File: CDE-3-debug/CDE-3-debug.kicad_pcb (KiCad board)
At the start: 2 copper layers, 101 x 86.4 mm, 79 parts

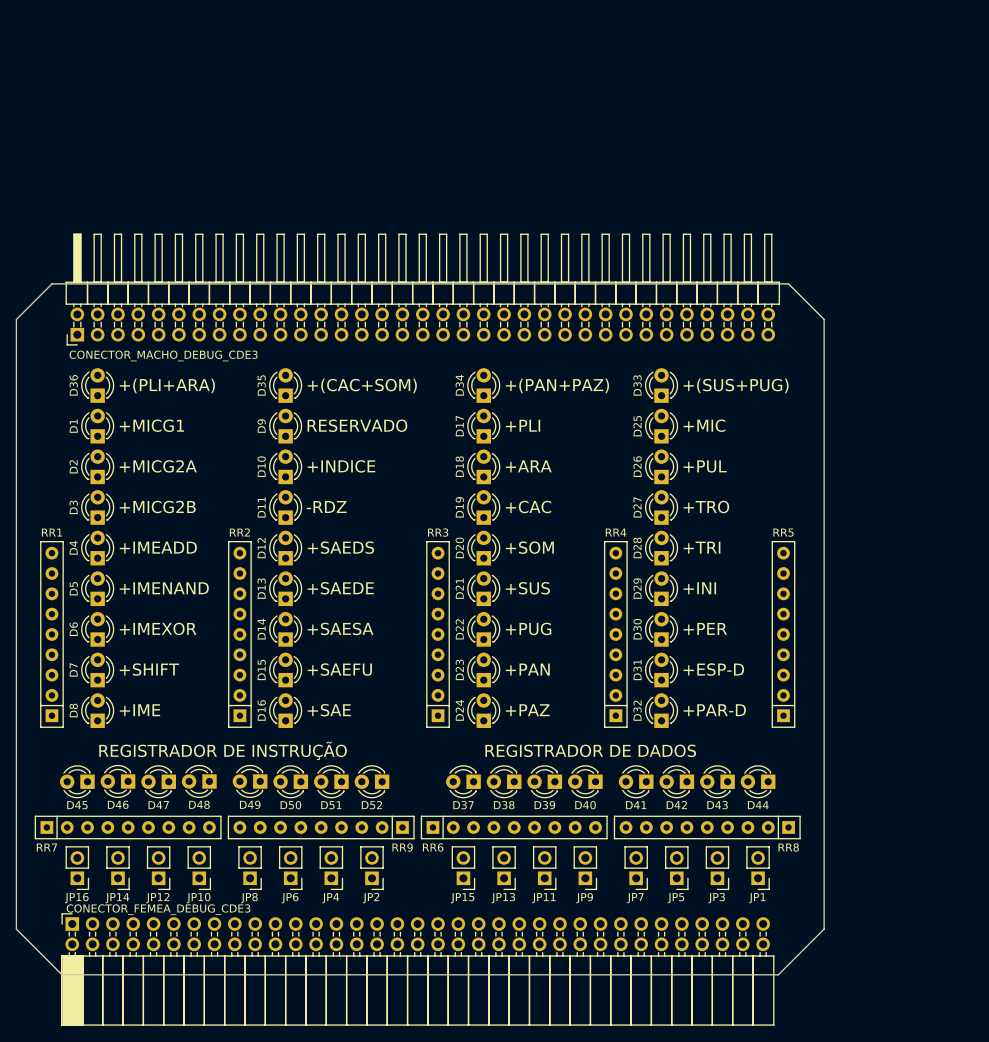
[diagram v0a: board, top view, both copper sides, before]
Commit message: trocando posição dos conectores macho/femea
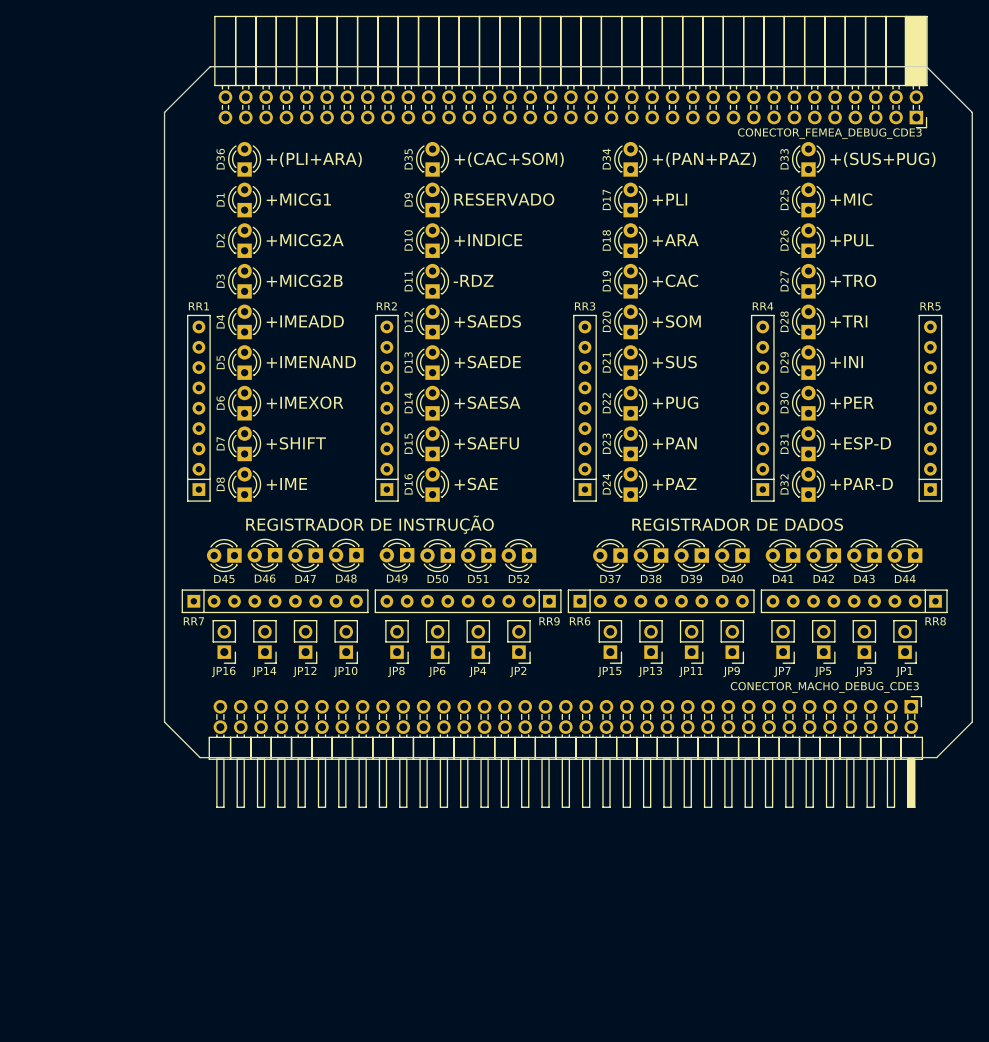
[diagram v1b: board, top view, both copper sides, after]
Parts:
- moved CONECTOR_FEMEA_DEBUG_CDE3 145.9 mm to (156.3, 80.8), turned to 270 degrees
- moved CONECTOR_MACHO_DEBUG_CDE3 114.1 mm to (155.7, 154.5), turned to 270 degrees
- moved JP5 33.7 mm to (144.7, 147.6)
- moved D25 33.7 mm to (142.8, 92.4)
- moved D26 33.7 mm to (142.8, 97.5)
- moved D27 33.7 mm to (142.8, 102.5)
- moved D30 33.7 mm to (142.8, 117.8)
- moved D32 33.7 mm to (142.8, 127.9)
- moved D37 33.7 mm to (119.3, 135.6)
- moved D38 33.7 mm to (124.4, 135.6)
- moved D39 33.7 mm to (129.5, 135.6)
- moved D41 33.7 mm to (140.9, 135.6)
- moved D43 33.7 mm to (151.1, 135.6)
- moved D44 33.7 mm to (156.2, 135.6)
- moved D45 33.7 mm to (71.1, 135.6)
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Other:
- outline, holes or cut-outs redrawn

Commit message: improvements to the CDE-3 and CDE-3-debug boards
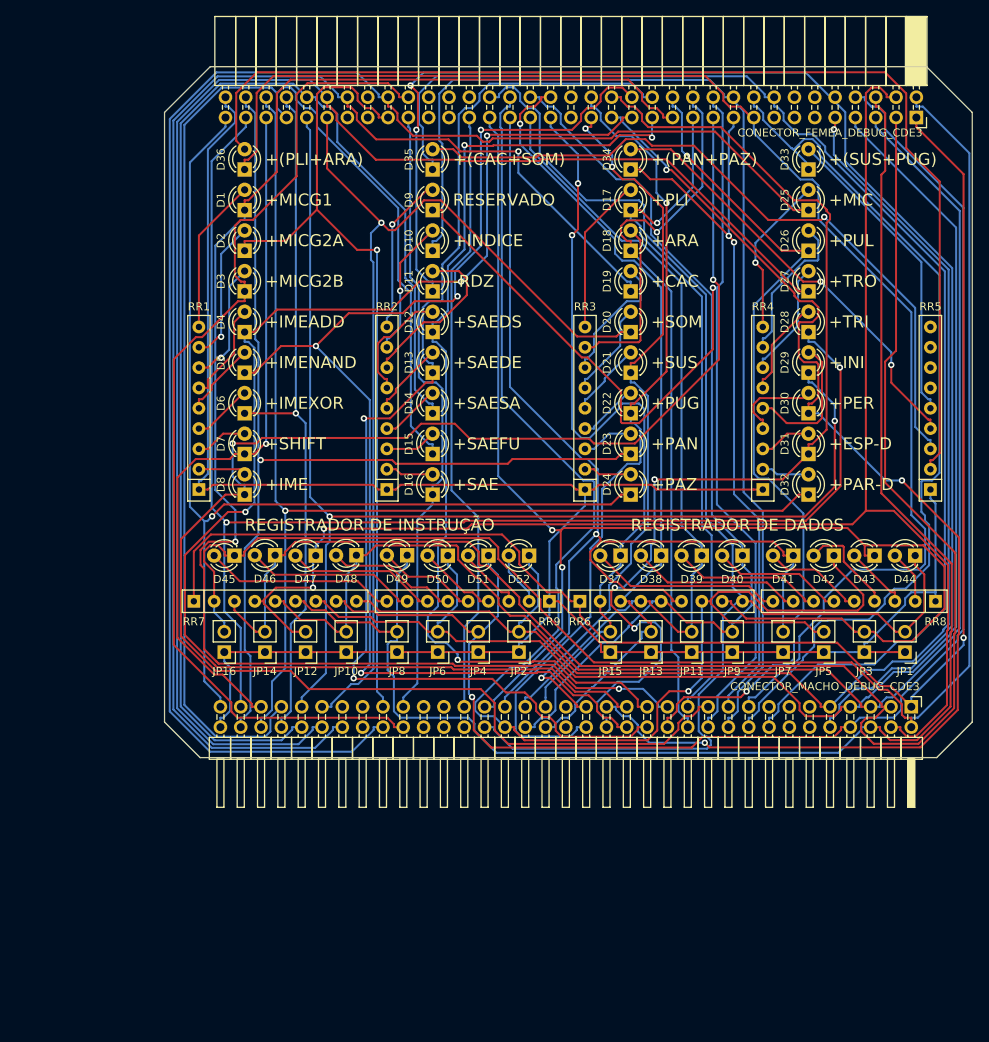
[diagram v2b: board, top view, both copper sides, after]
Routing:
- net GND: track 0.00 -> 270.0 mm
- net +IME: track 0.00 -> 203.5 mm, vias 0 -> 2
- net +RI_1: track 0.00 -> 201.5 mm
- net +RI_0: track 0.00 -> 200.0 mm
- net +MIC: track 0.00 -> 196.1 mm
- net +RI_4: track 0.00 -> 192.9 mm
- net +MICG1: track 0.00 -> 192.3 mm, vias 0 -> 2
- net +RI_2: track 0.00 -> 189.3 mm, vias 0 -> 2
- net +TRO: track 0.00 -> 187.8 mm
- net +RI_6: track 0.00 -> 187.2 mm, vias 0 -> 1
- net VCC: track 0.00 -> 186.5 mm, vias 0 -> 1
- net +RD_5: track 0.00 -> 180.6 mm, vias 0 -> 1
- net +RI_3: track 0.00 -> 179.2 mm
- net +TRI: track 0.00 -> 177.1 mm, vias 0 -> 2
- net -RDZ: track 0.00 -> 176.6 mm, vias 0 -> 2
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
